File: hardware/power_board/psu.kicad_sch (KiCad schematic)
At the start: 10 parts, among them U8 AMS1117-3.3

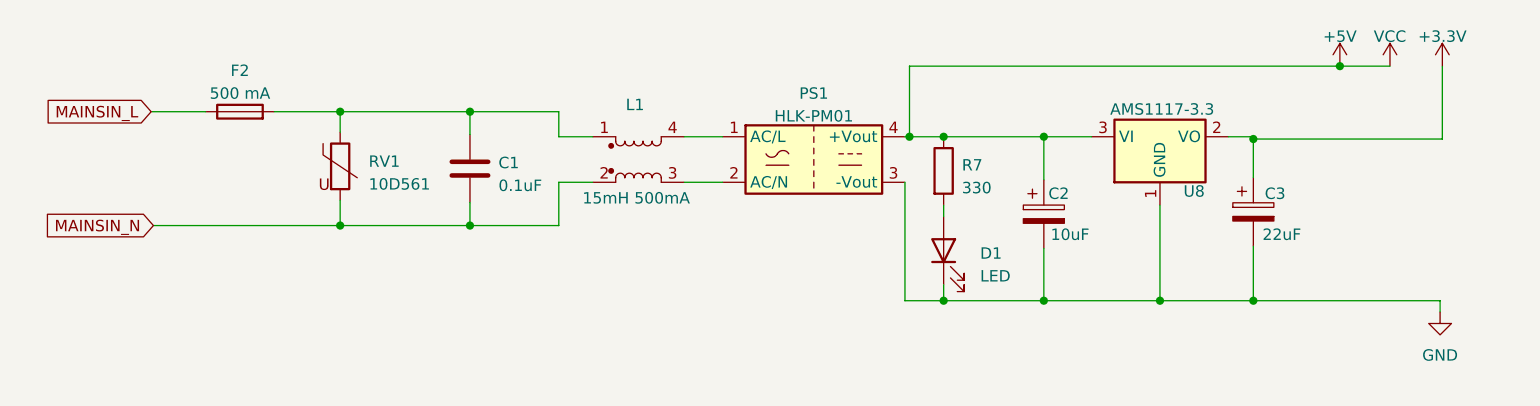
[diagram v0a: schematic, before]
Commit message: v2 Power/Relay PCB
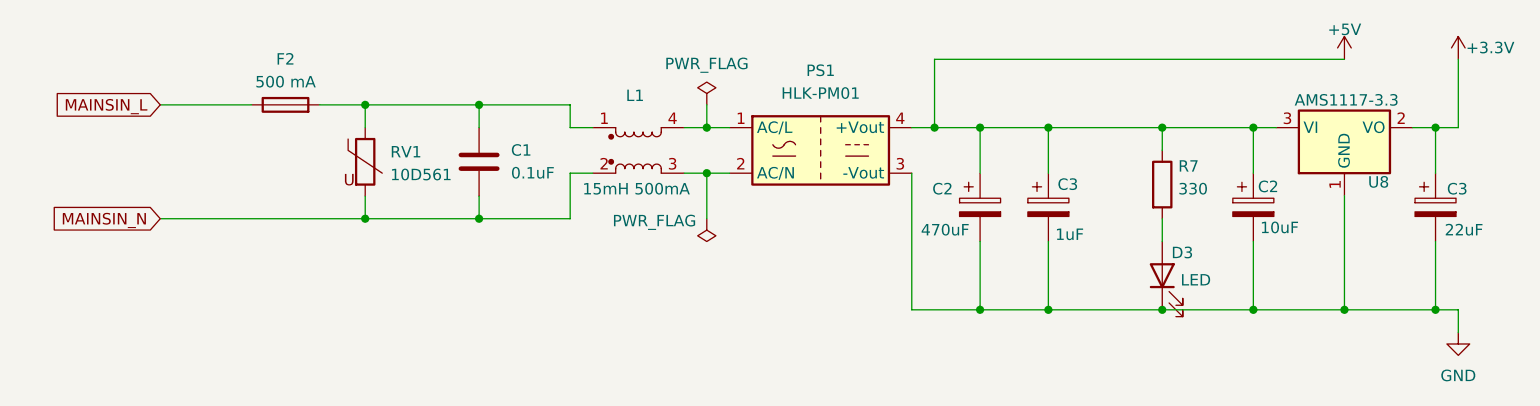
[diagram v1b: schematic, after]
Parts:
- added C2: 470uF, Capacitor_THT:CP_Radial_D8.0mm_P3.50mm, symbol Device:C_Polarized
- added C3: 1uF, Capacitor_THT:CP_Radial_D8.0mm_P3.50mm, symbol Device:C_Polarized
- D3: renamed from D1; footprint LED_THT:LED_D5.0mm_Clear -> LED_SMD:LED_0805_2012Metric_Pad1.15x1.40mm_HandSolder
- F2: footprint TE5:FUSE_BK_PCE-5-R -> Fuse:Fuse_Littelfuse_395Series
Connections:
- net +5V: now also C2.1, C3.1
- net GND: now also C2.2, C3.2
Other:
- moved on the sheet: C1, C2, C3, D3, F2, L1, PS1, R7, RV1, U8

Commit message: Refactored PCBs for v2. See README
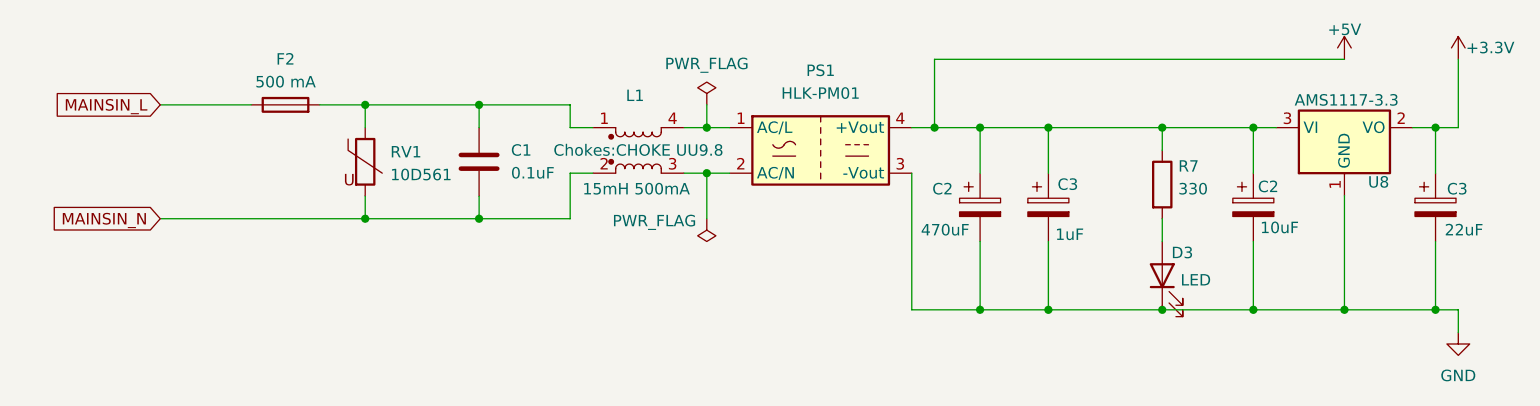
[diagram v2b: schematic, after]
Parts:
- L1: footprint Inductor_THT:Choke_Schaffner_RN204-04-9.0x14.0mm -> Chokes:CHOKE UU9.8
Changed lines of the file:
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@@
       (effects (font (size 1.27 1.27)))
     )
-    (property "Footprint" "Inductor_THT:Choke_Schaffner_RN204-04-9.0x14.0mm" (at 129.54 91.44 0)
-      (effects (font (size 1.27 1.27)) hide)
+    (property "Footprint" "Chokes:CHOKE UU9.8" (at 129.54 91.44 0)
+      (effects (font (size 1.27 1.27)))
     )
     (property "Datasheet" "~" (at 129.54 91.44 0)
